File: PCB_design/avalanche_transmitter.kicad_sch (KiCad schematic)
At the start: 8 parts, among them J1 Conn_01x07_Pin, Q1 2N3904, U1 74HC00

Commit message: Add files via upload
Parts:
- removed U3: ~, ta:pro_mini, symbol ta:pro_mini
- added D1: RED_LED_25, LED_THT:LED_D5.0mm, symbol Device:LED
- added D2: RED_LED_50, LED_THT:LED_D5.0mm, symbol Device:LED
- added D3: RED_LED_75, LED_THT:LED_D5.0mm, symbol Device:LED
- added D4: RED_LED_100, LED_THT:LED_D5.0mm, symbol Device:LED
- added D5: GREEN_LED, LED_THT:LED_D5.0mm, symbol Device:LED
- added R1, R2, R3, R4, R5, R6: R_Small, Resistor_THT:R_Axial_DIN0204_L3.6mm_D1.6mm_P7.62mm_Horizontal, symbol Device:R_Small
- added SW1: SW_Push, symbol Switch:SW_Push
- added U2: ~, ta:pro_mini, symbol ta:pro_mini
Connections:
- net +3V0: now also U2.4 (3V)
- net +6V: now also U2.1 (bat)
- net GND: now also R1.2, R2.2, R3.2, R4.2, R5.2, R6.2, SW1.2, U2.2 (ground)
- net at U1.2: now also U2.16 (12)
- net at J1.5 (Pin_5): now also U2.23 (A4)
- net at J1.4 (Pin_4): now also U2.24 (A5)
- new net: D5.1 (K), U2.17 (13)
- new net: D5.2 (A), R5.1
- new net: D2.1 (K), U2.7 (5)
- new net: D2.2 (A), R2.1
- new net: D3.2 (A), R3.1
- new net: D1.2 (A), R1.1
- new net: D4.2 (A), R4.1
- new net: R6.1, SW1.1, U2.5 (8)
- new net: D3.1 (K), U2.8 (4)
- new net: D4.1 (K), U2.9 (3)
- new net: D1.1 (K), U2.6

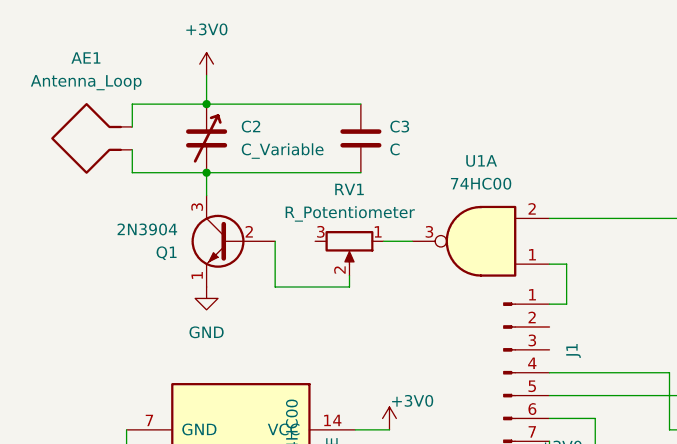
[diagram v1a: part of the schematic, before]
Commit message: PCB updates
Added some vias, rerouted some things, changed the footprint for the SI
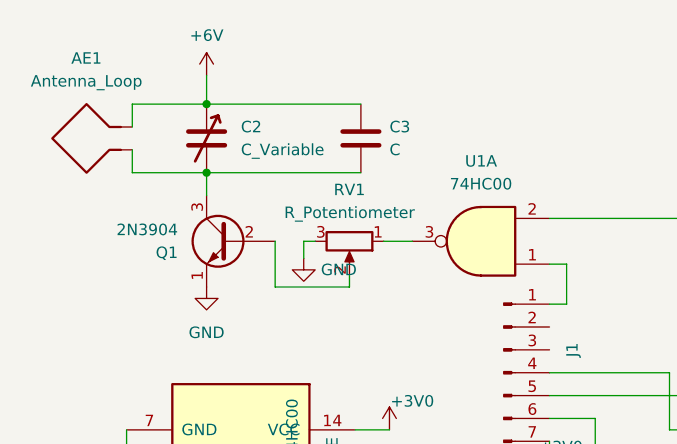
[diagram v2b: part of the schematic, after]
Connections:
- net +3V0: no longer AE1.2, C2.1, C3.1
- net +6V: now also AE1.2, C2.1, C3.1
- net GND: now also RV1.3
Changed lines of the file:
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@@
+    (stroke (width 0) (type default))
+  )
+  (wire (pts (xy 95.885 41.275) (xy 94.615 41.275))
     (stroke (width 0) (type default))
   )
@@
     (stroke (width 0) (type default))
   )
+  (wire (pts (xy 94.615 41.275) (xy 94.615 43.18))
+    (stroke (width 0) (type default))
+  )
   (wire (pts (xy 180.34 44.45) (xy 187.96 44.45))
     (stroke (width 0) (type default))
@@
   (wire (pts (xy 196.85 35.56) (xy 196.85 39.37))
     (stroke (width 0) (type default))
+  )
+  (symbol (lib_id "power:+6V") (at 83.82 22.86 0) (unit 1)
+    (in_bom yes) (on_board yes) (dnp no) (fields_autoplaced)
+    (property "Reference" "#PWR07" (at 83.82 26.67 0)
+      (effects (font (size 1.27 1.27)) hide)
+    )
+    (property "Value" "+6V" (at 83.82 18.415 0)
+      (effects (font (size 1.27 1.27)))
+    )
+    (property "Footprint" "" (at 83.82 22.86 0)
+      (effects (font (size 1.27 1.27)) hide)
+    )
+    (property "Datasheet" "" (at 83.82 22.86 0)
+      (effects (font (size 1.27 1.27)) hide)
+    )
+    (pin "1")
+    (instances
+      (project "avalanche_transmitter"
+        (path "/8c884e5d-9429-461a-a115-9f5a3e16f11a"
+          (reference "#PWR07") (unit 1)
+        )
+      )
+    )
   )
   (symbol (lib_id "power:+3V0") (at 120.65 67.31 0) (unit 1)
@@
         (path "/8c884e5d-9429-461a-a115-9f5a3e16f11a"
           (reference "Q1") (unit 1)
-        )
-      )
-    )
-  )
-  (symbol (lib_id "power:+3V0") (at 83.82 22.86 0) (unit 1)
-    (in_bom yes) (on_board yes) (dnp no) (fields_autoplaced)
-    (property "Reference" "#PWR07" (at 83.82 26.67 0)
-      (effects (font (size 1.27 1.27)) hide)
-    )
-    (property "Value" "+3V0" (at 83.82 17.78 0)
-      (effects (font (size 1.27 1.27)))
-    )
-    (property "Footprint" "" (at 83.82 22.86 0)
-      (effects (font (size 1.27 1.27)) hide)
-    )
-    (property "Datasheet" "" (at 83.82 22.86 0)
-      (effects (font (size 1.27 1.27)) hide)
-    )
-    (pin "1")
-    (instances
-      (project "avalanche_transmitter"
-        (path "/8c884e5d-9429-461a-a115-9f5a3e16f11a"
-          (reference "#PWR07") (unit 1)
         )
       )
@@
         )
       )
+    )
+  )
+  (symbol (lib_id "power:GND") (at 94.615 43.18 0) (unit 1)
+    (in_bom yes) (on_board yes) (dnp no) (fields_autoplaced)
+    (property "Reference" "#PWR011" (at 94.615 49.53 0)
+      (effects (font (size 1.27 1.27)) hide)
+    )
+    (property "Value" "GND" (at 96.52 44.45 0)
+      (effects (font (size 1.27 1.27)) (justify left))
+    )
+    (property "Footprint" "" (at 94.615 43.18 0)
+      (effects (font (size 1.27 1.27)) hide)
+    )
+    (property "Datasheet" "" (at 94.615 43.18 0)
+      (effects (font (size 1.27 1.27)) hide)
+    )
+    (pin "1")
+    (instances
+      (project "avalanche_transmitter"
+        (path "/8c884e5d-9429-461a-a115-9f5a3e16f11a"
+          (reference "#PWR011") (unit 1)
+        )
+      )

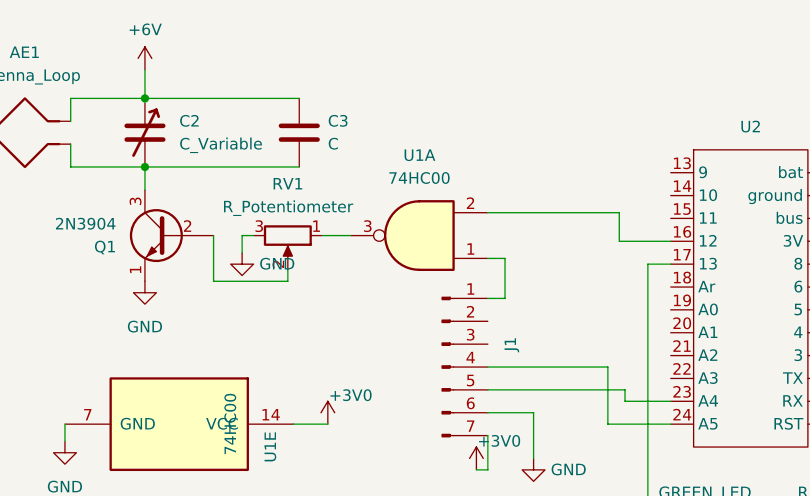
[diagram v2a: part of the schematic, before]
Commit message: added series resistor to increase magfield
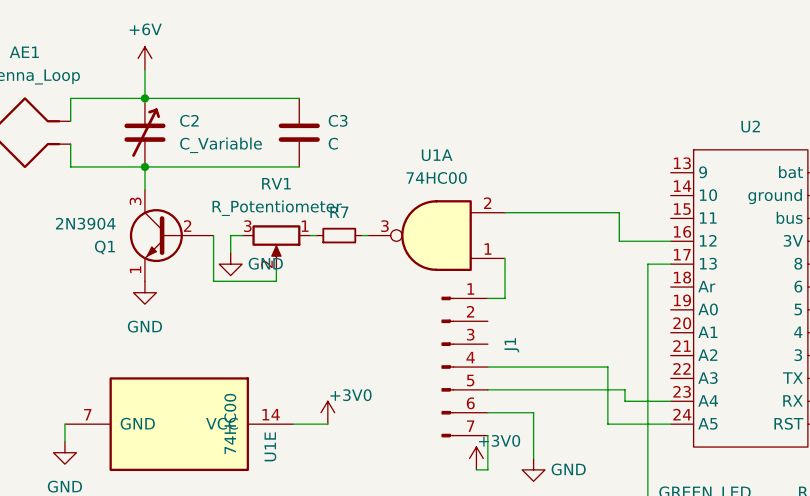
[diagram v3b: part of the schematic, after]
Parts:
- added R7: R_Small, Resistor_THT:R_Axial_DIN0204_L3.6mm_D1.6mm_P7.62mm_Horizontal, symbol Device:R_Small
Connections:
- net at RV1.1: now also R7.1; no longer U1.3
- new net: R7.2, U1.3
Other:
- moved on the sheet: RV1, U1A
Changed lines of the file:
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@@
     (stroke (width 0) (type default))
   )
-  (wire (pts (xy 95.885 41.275) (xy 94.615 41.275))
+  (wire (pts (xy 94.615 41.275) (xy 93.345 41.275))
     (stroke (width 0) (type default))
   )
@@
     (stroke (width 0) (type default))
   )
-  (wire (pts (xy 121.92 38.735) (xy 136.525 38.735))
+  (wire (pts (xy 123.825 38.735) (xy 136.525 38.735))
     (stroke (width 0) (type default))
   )
@@
     (stroke (width 0) (type default))
   )
-  (wire (pts (xy 99.695 46.355) (xy 91.44 46.355))
+  (wire (pts (xy 98.425 46.355) (xy 91.44 46.355))
     (stroke (width 0) (type default))
   )
@@
     (stroke (width 0) (type default))
   )
-  (wire (pts (xy 99.695 45.085) (xy 99.695 46.355))
+  (wire (pts (xy 98.425 45.085) (xy 98.425 46.355))
     (stroke (width 0) (type default))
   )
@@
     (stroke (width 0) (type default))
   )
-  (wire (pts (xy 121.92 43.815) (xy 123.825 43.815))
-    (stroke (width 0) (type default))
-  )
   (wire (pts (xy 180.34 59.69) (xy 187.96 59.69))
     (stroke (width 0) (type default))
@@
     (stroke (width 0) (type default))
   )
+  (wire (pts (xy 107.95 41.275) (xy 108.585 41.275))
+    (stroke (width 0) (type default))
+  )
   (wire (pts (xy 137.16 59.69) (xy 142.24 59.69))
     (stroke (width 0) (type default))
@@
     (stroke (width 0) (type default))
   )
-  (wire (pts (xy 103.505 41.275) (xy 106.68 41.275))
-    (stroke (width 0) (type default))
-  )
   (wire (pts (xy 75.565 31.115) (xy 75.565 33.655))
     (stroke (width 0) (type default))
   )
-  (wire (pts (xy 94.615 41.275) (xy 94.615 43.18))
+  (wire (pts (xy 93.345 41.275) (xy 93.345 43.18))
+    (stroke (width 0) (type default))
+  )
+  (wire (pts (xy 102.235 41.275) (xy 102.87 41.275))
     (stroke (width 0) (type default))
   )
@@
     )
   )
+  (symbol (lib_id "Device:R_Small") (at 105.41 41.275 90) (unit 1)
+    (in_bom yes) (on_board yes) (dnp no) (fields_autoplaced)
+    (property "Reference" "R7" (at 105.41 38.735 90)
+      (effects (font (size 1.27 1.27)))
+    )
+    (property "Value" "R_Small" (at 105.41 38.735 90)
+      (effects (font (size 1.27 1.27)) hide)
+    )
+    (property "Footprint" "Resistor_THT:R_Axial_DIN0204_L3.6mm_D1.6mm_P7.62mm_Horizontal" (at 105.41 41.275 0)
+      (effects (font (size 1.27 1.27)) hide)
+    )
+    (property "Datasheet" "~" (at 105.41 41.275 0)
+      (effects (font (size 1.27 1.27)) hide)
+    )
+    (pin "1")
+    (pin "2")
+    (instances
+      (project "avalanche_transmitter"
+        (path "/8c884e5d-9429-461a-a115-9f5a3e16f11a"
+          (reference "R7") (unit 1)
+        )
+      )
+    )
+  )
   (symbol (lib_id "Device:C") (at 100.965 29.845 0) (unit 1)
     (in_bom yes) (on_board yes) (dnp no) (fields_autoplaced)
@@
     )
   )
-  (symbol (lib_id "74xx:74HC00") (at 114.3 41.275 180) (unit 1)
-    (in_bom yes) (on_board yes) (dnp no) (fields_autoplaced)
-    (property "Reference" "U1" (at 114.3083 32.385 0)
-      (effects (font (size 1.27 1.27)))
-    )
-    (property "Value" "74HC00" (at 114.3083 34.925 0)
-      (effects (font (size 1.27 1.27)))
-    )
-    (property "Footprint" "Package_DIP:DIP-14_W7.62mm" (at 114.3 41.275 0)
-      (effects (font (size 1.27 1.27)) hide)
-    )
-    (property "Datasheet" "http://www.ti.com/lit/gpn/sn74hc00" (at 114.3 41.275 0)
+  (symbol (lib_id "74xx:74HC00") (at 116.205 41.275 180) (unit 1)
+    (in_bom yes) (on_board yes) (dnp no) (fields_autoplaced)
+    (property "Reference" "U1" (at 116.2133 32.385 0)
+      (effects (font (size 1.27 1.27)))
+    )
+    (property "Value" "74HC00" (at 116.2133 34.925 0)
+      (effects (font (size 1.27 1.27)))
+    )
+    (property "Footprint" "Package_DIP:DIP-14_W7.62mm" (at 116.205 41.275 0)
+      (effects (font (size 1.27 1.27)) hide)
+    )
+    (property "Datasheet" "http://www.ti.com/lit/gpn/sn74hc00" (at 116.205 41.275 0)
       (effects (font (size 1.27 1.27)) hide)
     )
@@
     )
   )
-  (symbol (lib_id "power:GND") (at 94.615 43.18 0) (unit 1)
-    (in_bom yes) (on_board yes) (dnp no) (fields_autoplaced)
-    (property "Reference" "#PWR011" (at 94.615 49.53 0)
-      (effects (font (size 1.27 1.27)) hide)
-    )
-    (property "Value" "GND" (at 96.52 44.45 0)
+  (symbol (lib_id "power:GND") (at 93.345 43.18 0) (unit 1)
+    (in_bom yes) (on_board yes) (dnp no) (fields_autoplaced)
+    (property "Reference" "#PWR011" (at 93.345 49.53 0)
+      (effects (font (size 1.27 1.27)) hide)
+    )
+    (property "Value" "GND" (at 95.25 44.45 0)
       (effects (font (size 1.27 1.27)) (justify left))
     )
-    (property "Footprint" "" (at 94.615 43.18 0)
-      (effects (font (size 1.27 1.27)) hide)
-    )
-    (property "Datasheet" "" (at 94.615 43.18 0)
+    (property "Footprint" "" (at 93.345 43.18 0)
+      (effects (font (size 1.27 1.27)) hide)
+    )
+    (property "Datasheet" "" (at 93.345 43.18 0)
       (effects (font (size 1.27 1.27)) hide)
     )
@@
     )
   )
-  (symbol (lib_id "Device:R_Potentiometer") (at 99.695 41.275 270) (unit 1)
-    (in_bom yes) (on_board yes) (dnp no) (fields_autoplaced)
-    (property "Reference" "RV1" (at 99.695 35.56 90)
-      (effects (font (size 1.27 1.27)))
-    )
-    (property "Value" "R_Potentiometer" (at 99.695 38.1 90)
-      (effects (font (size 1.27 1.27)))
-    )
-    (property "Footprint" "Potentiometer_THT:Potentiometer_Bourns_3296W_Vertical" (at 99.695 41.275 0)
-      (effects (font (size 1.27 1.27)) hide)
-    )
-    (property "Datasheet" "~" (at 99.695 41.275 0)
-      (effects (font (size 1.27 1.27)) hide)
-    )
+  (symbol (lib_id "Device:R_Potentiometer") (at 98.425 41.275 270) (unit 1)
+    (in_bom yes) (on_board yes) (dnp no) (fields_autoplaced)
+    (property "Reference" "RV1" (at 98.425 35.56 90)
+      (effects (font (size 1.27 1.27)))
+    )
+    (property "Value" "R_Potentiometer" (at 98.425 38.1 90)
+      (effects (font (size 1.27 1.27)))
+    )
+    (property "Footprint" "Potentiometer_THT:Potentiometer_Bourns_3296W_Vertical" (at 98.425 41.275 0)
+      (effects (font (size 1.27 1.27)) hide)
+    )
+    (property "Datasheet" "~" (at 98.425 41.275 0)
+      (effects (font (size 1.27 1.27)) hide)
+    )

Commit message: finished PCB. ready for bens review
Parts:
- renumbered D4 to 100%, D2 to 50%, D3 to 75%, D5 to TRANSMITTING
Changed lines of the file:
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@@
   (symbol (lib_id "Device:LED") (at 146.05 72.39 0) (unit 1)
     (in_bom yes) (on_board yes) (dnp no)
-    (property "Reference" "D5" (at 149.86 69.85 0)
+    (property "Reference" "TRANSMITTING" (at 149.86 69.85 0)
       (effects (font (size 1.27 1.27)) hide)
     )
@@
       (project "avalanche_transmitter"
         (path "/8c884e5d-9429-461a-a115-9f5a3e16f11a"
-          (reference "D5") (unit 1)
+          (reference "TRANSMITTING") (unit 1)
         )
       )
@@
   (symbol (lib_id "Device:LED") (at 176.53 52.07 0) (unit 1)
     (in_bom yes) (on_board yes) (dnp no)
-    (property "Reference" "D2" (at 180.34 49.53 0)
+    (property "Reference" "50%" (at 180.34 49.53 0)
       (effects (font (size 1.27 1.27)) hide)
     )
@@
       (project "avalanche_transmitter"
         (path "/8c884e5d-9429-461a-a115-9f5a3e16f11a"
-          (reference "D2") (unit 1)
+          (reference "50%") (unit 1)
         )
       )
@@
   (symbol (lib_id "Device:LED") (at 176.53 59.69 0) (unit 1)
     (in_bom yes) (on_board yes) (dnp no)
-    (property "Reference" "D3" (at 180.34 57.15 0)
+    (property "Reference" "75%" (at 180.34 57.15 0)
       (effects (font (size 1.27 1.27)) hide)
     )
@@
       (project "avalanche_transmitter"
         (path "/8c884e5d-9429-461a-a115-9f5a3e16f11a"
-          (reference "D3") (unit 1)
+          (reference "75%") (unit 1)
         )
       )
@@
   (symbol (lib_id "Device:LED") (at 176.53 66.04 0) (unit 1)
     (in_bom yes) (on_board yes) (dnp no)
-    (property "Reference" "D4" (at 180.34 63.5 0)
+    (property "Reference" "100%" (at 180.34 63.5 0)
       (effects (font (size 1.27 1.27)) hide)
     )
@@
       (project "avalanche_transmitter"
         (path "/8c884e5d-9429-461a-a115-9f5a3e16f11a"
-          (reference "D4") (unit 1)
-        )
-      )
+          (reference "100%") (unit 1)
+        )
+      )

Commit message: updated layout. ready for review again
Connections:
- net +3V0: now also SW1.2
- net GND: no longer SW1.2
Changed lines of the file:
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@@
 (kicad_sch (version 20230121) (generator eeschema)
   (paper "A4")
-  (junction (at 196.85 39.37) (diameter 0) (color 0 0 0 0)
-  )
   (junction (at 196.85 44.45) (diameter 0) (color 0 0 0 0)
   )
@@
     (stroke (width 0) (type default))
   )
+  (wire (pts (xy 195.58 35.56) (xy 195.58 33.02))
+    (stroke (width 0) (type default))
+  )
   (wire (pts (xy 139.7 72.39) (xy 139.7 44.45))
     (stroke (width 0) (type default))
@@
     (stroke (width 0) (type default))
   )
-  (wire (pts (xy 189.23 35.56) (xy 196.85 35.56))
+  (wire (pts (xy 189.23 35.56) (xy 195.58 35.56))
     (stroke (width 0) (type default))
   )
@@
     (stroke (width 0) (type default))
   )
-  (wire (pts (xy 196.85 35.56) (xy 196.85 39.37))
-    (stroke (width 0) (type default))
-  )
   (symbol (lib_id "power:+6V") (at 83.82 22.86 0) (unit 1)
     (in_bom yes) (on_board yes) (dnp no) (fields_autoplaced)
@@
         (path "/8c884e5d-9429-461a-a115-9f5a3e16f11a"
           (reference "#PWR08") (unit 1)
+        )
+      )
+    )
+  )
+  (symbol (lib_id "power:+3V0") (at 195.58 33.02 0) (unit 1)
+    (in_bom yes) (on_board yes) (dnp no)
+    (property "Reference" "#PWR012" (at 195.58 36.83 0)
+      (effects (font (size 1.27 1.27)) hide)
+    )
+    (property "Value" "+3V0" (at 198.12 29.845 0)
+      (effects (font (size 1.27 1.27)))
+    )
+    (property "Footprint" "" (at 195.58 33.02 0)
+      (effects (font (size 1.27 1.27)) hide)
+    )
+    (property "Datasheet" "" (at 195.58 33.02 0)
+      (effects (font (size 1.27 1.27)) hide)
+    )
+    (pin "1")
+    (instances
+      (project "avalanche_transmitter"
+        (path "/8c884e5d-9429-461a-a115-9f5a3e16f11a"
+          (reference "#PWR012") (unit 1)
         )
       )
@@
   )
   (symbol (lib_id "power:GND") (at 162.56 38.1 0) (unit 1)
-    (in_bom yes) (on_board yes) (dnp no) (fields_autoplaced)
+    (in_bom yes) (on_board yes) (dnp no)
     (property "Reference" "#PWR02" (at 162.56 44.45 0)
       (effects (font (size 1.27 1.27)) hide)
     )
-    (property "Value" "GND" (at 162.56 43.18 0)
-      (effects (font (size 1.27 1.27)))
-    )
+    (property "Value" "GND" (at 162.56 35.56 0)
+      (effects (font (size 1.27 1.27)))
+    )

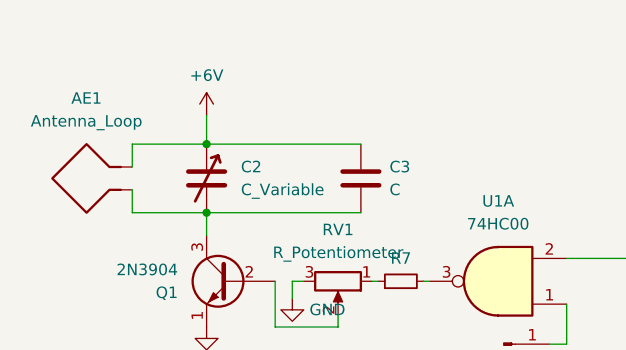
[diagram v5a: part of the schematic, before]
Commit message: adjusted pin connectors on PCB to lead to vias with red wires
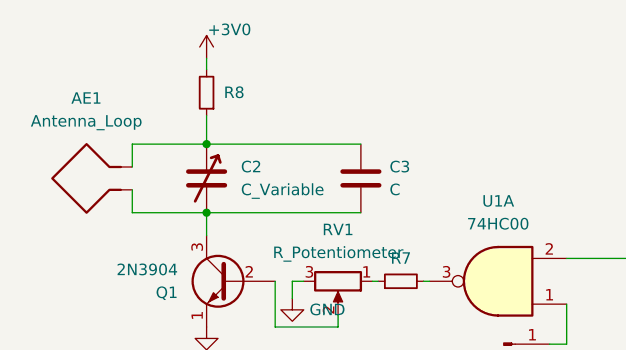
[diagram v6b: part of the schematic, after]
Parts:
- added R8: R_Small, Resistor_THT:R_Axial_DIN0204_L3.6mm_D1.6mm_P7.62mm_Horizontal, symbol Device:R_Small
- renumbered 100% to 100%1, 50% to 50%1, 75% to 75%1, TRANSMITTING to TRANSMITTING1
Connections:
- net +3V0: now also R8.2
- net +6V: no longer AE1.2, C2.1, C3.1
- new net: AE1.2, C2.1, C3.1, R8.1
